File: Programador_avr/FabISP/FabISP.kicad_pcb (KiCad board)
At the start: 2 copper layers, 43.5 x 25 mm, 18 parts, among them IC1 ATTINY44-SSU, M1 20MHz, M2 PINHD-1x02-SMD-HEADER, M3 MICRO-USB_1_64

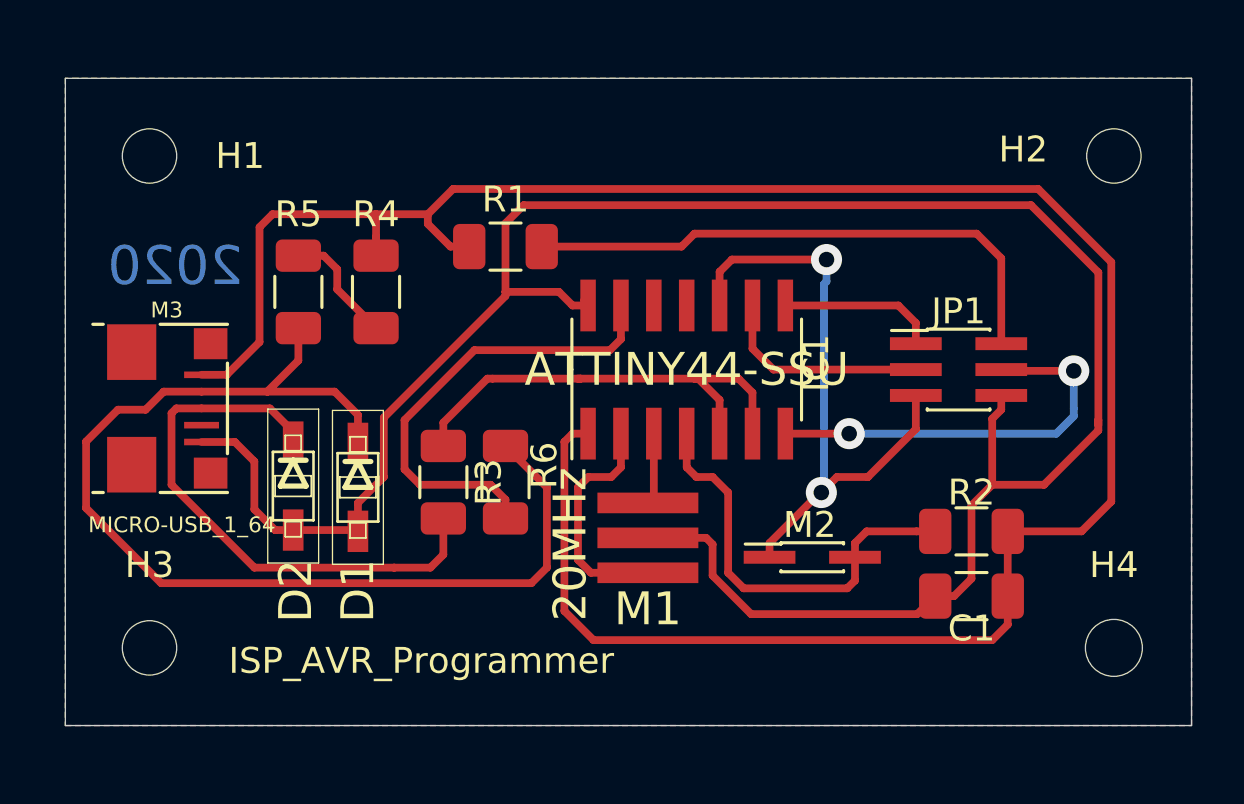
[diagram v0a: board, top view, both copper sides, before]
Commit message: comentatios DWgs, Corrección de margendes
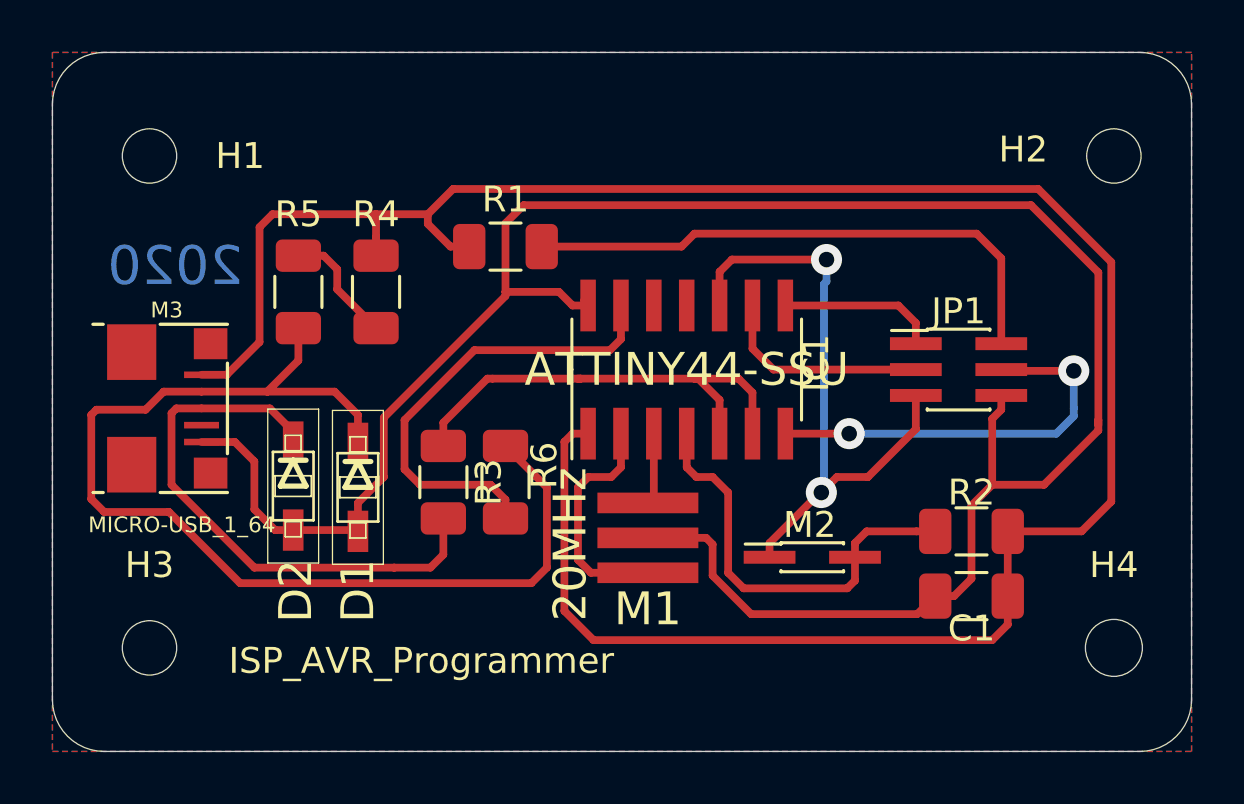
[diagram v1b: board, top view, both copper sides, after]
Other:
- board size 43.5 x 25 mm -> 44 x 27 mm
- rule trace_min: 0.2 -> 0.25
- board text added: "Vía 1.2mm/0.6mm"
- board text added: "grilla de borde : 1mm grilla de componentes: 0.25mm grilla pistas 0.25mm"
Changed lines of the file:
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@@
   (general
     (thickness 1.6)
-    (drawings 8)
-    (tracks 176)
+    (drawings 15)
+    (tracks 178)
     (zones 0)
     (modules 18)
@@
   )
   (setup
-    (last_trace_width 0.25)
+    (last_trace_width 0.3)
     (user_trace_width 0.3)
     (trace_clearance 0.2)
     (zone_clearance 0.508)
     (zone_45_only no)
-    (trace_min 0.2)
+    (trace_min 0.25)
     (via_size 0.8)
     (via_drill 0.4)
@@
     (pad "" np_thru_hole circle (at 0 0) (size 2.1 2.1) (drill 2.1) (layers *.Cu *.Mask))
   )
-  (gr_line (start 125.5 84) (end 126 84) (layer Edge.Cuts) (width 0.05))
-  (gr_line (start 125.5 109) (end 125.5 84) (layer Edge.Cuts) (width 0.05))
-  (gr_line (start 126 109) (end 125.5 109) (layer Edge.Cuts) (width 0.05))
-  (gr_line (start 126 109) (end 169 109) (layer Edge.Cuts) (width 0.05))
-  (gr_line (start 169 84) (end 126 84) (layer Edge.Cuts) (width 0.05))
-  (gr_line (start 169 84) (end 169 109) (layer Edge.Cuts) (width 0.05))
+  (dimension 2 (width 0.15) (layer Dwgs.User)
+    (gr_text "2,000 mm" (at 168 114.3) (layer Dwgs.User)
+      (effects (font (size 1 1) (thickness 0.15)))
+    )
+    (feature1 (pts (xy 169 108) (xy 169 113.586421)))
+    (feature2 (pts (xy 167 108) (xy 167 113.586421)))
+    (crossbar (pts (xy 167 113) (xy 169 113)))
+    (arrow1a (pts (xy 169 113) (xy 167.873496 113.586421)))
+    (arrow1b (pts (xy 169 113) (xy 167.873496 112.413579)))
+    (arrow2a (pts (xy 167 113) (xy 168.126504 113.586421)))
+    (arrow2b (pts (xy 167 113) (xy 168.126504 112.413579)))
+  )
+  (dimension 27 (width 0.15) (layer Dwgs.User)
+    (gr_text "27,000 mm" (at 120.7 96.5 270) (layer Dwgs.User)
+      (effects (font (size 1 1) (thickness 0.15)))
+    )
+    (feature1 (pts (xy 127 110) (xy 121.413579 110)))
+    (feature2 (pts (xy 127 83) (xy 121.413579 83)))
+    (crossbar (pts (xy 122 83) (xy 122 110)))
+    (arrow1a (pts (xy 122 110) (xy 121.413579 108.873496)))
+    (arrow1b (pts (xy 122 110) (xy 122.586421 108.873496)))
+    (arrow2a (pts (xy 122 83) (xy 121.413579 84.126504)))
+    (arrow2b (pts (xy 122 83) (xy 122.586421 84.126504)))
+  )
+  (dimension 44 (width 0.15) (layer Dwgs.User)
+    (gr_text "44,000 mm" (at 147 80.7) (layer Dwgs.User)
+      (effects (font (size 1 1) (thickness 0.15)))
+    )
+    (feature1 (pts (xy 169 85) (xy 169 81.413579)))
+    (feature2 (pts (xy 125 85) (xy 125 81.413579)))
+    (crossbar (pts (xy 125 82) (xy 169 82)))
+    (arrow1a (pts (xy 169 82) (xy 167.873496 82.586421)))
+    (arrow1b (pts (xy 169 82) (xy 167.873496 81.413579)))
+    (arrow2a (pts (xy 125 82) (xy 126.126504 82.586421)))
+    (arrow2b (pts (xy 125 82) (xy 126.126504 81.413579)))
+  )
+  (gr_text "Vía 1.2mm/0.6mm" (at 179 93) (layer Dwgs.User)
+    (effects (font (size 1 1) (thickness 0.15)))
+  )
+  (gr_line (start 125 108) (end 125 85) (layer Edge.Cuts) (width 0.05))
+  (gr_line (start 167 110) (end 127 110) (layer Edge.Cuts) (width 0.05))
+  (gr_line (start 169 85) (end 169 108) (layer Edge.Cuts) (width 0.05))
+  (gr_line (start 127 83) (end 167 83) (layer Edge.Cuts) (width 0.05))
+  (gr_arc (start 167 85) (end 169 85) (angle -90) (layer Edge.Cuts) (width 0.05))
+  (gr_arc (start 167 108) (end 167 110) (angle -90) (layer Edge.Cuts) (width 0.05))
+  (gr_arc (start 127 85) (end 127 83) (angle -90) (layer Edge.Cuts) (width 0.05))
+  (gr_arc (start 127 108) (end 125 108) (angle -90) (layer Edge.Cuts) (width 0.05))
+  (gr_text "grilla de borde : 1mm\ngrilla de componentes: 0.25mm\ngrilla pistas 0.25mm" (at 172 85) (layer Dwgs.User)
+    (effects (font (size 1 1) (thickness 0.15)) (justify left))
+  )
   (gr_text 2020 (at 129.75 91.25) (layer B.Cu)
     (effects (font (size 1.5 1.5) (thickness 0.3)) (justify mirror))
@@
   (segment (start 134.5 94.9) (end 134.5 93.65) (width 0.3) (layer F.Cu) (net 16) (status 20))
   (segment (start 133.2977 96.1023) (end 134.5 94.9) (width 0.3) (layer F.Cu) (net 16))
-  (segment (start 142.5 98.2) (end 144.1 99.8) (width 0.3) (layer F.Cu) (net 16) (status 10))
-  (segment (start 144.1 99.8) (end 144.1 102.9) (width 0.3) (layer F.Cu) (net 16))
-  (segment (start 144.1 102.9) (end 143.5 103.5) (width 0.3) (layer F.Cu) (net 16))
-  (segment (start 129.2 103.5) (end 126.3 100.6) (width 0.3) (layer F.Cu) (net 16))
-  (segment (start 143.5 103.5) (end 129.2 103.5) (width 0.3) (layer F.Cu) (net 16))
-  (segment (start 126.3 98.031959) (end 127.531959 96.8) (width 0.3) (layer F.Cu) (net 16))
-  (segment (start 126.3 100.6) (end 126.3 98.031959) (width 0.3) (layer F.Cu) (net 16))
-  (segment (start 127.531959 96.8) (end 128.6 96.8) (width 0.3) (layer F.Cu) (net 16))
-  (segment (start 129.2977 96.1023) (end 130.759581 96.1023) (width 0.3) (layer F.Cu) (net 16) (status 20))
-  (segment (start 128.6 96.8) (end 129.2977 96.1023) (width 0.3) (layer F.Cu) (net 16))
   (segment (start 135.90113 96.1023) (end 133.2977 96.1023) (width 0.3) (layer F.Cu) (net 16))
   (segment (start 136.8 97.00117) (end 135.90113 96.1023) (width 0.3) (layer F.Cu) (net 16))
   (segment (start 136.8 98.1) (end 136.8 97.00117) (width 0.3) (layer F.Cu) (net 16) (status 10))
+  (segment (start 129.2977 96.1023) (end 130.759581 96.1023) (width 0.3) (layer F.Cu) (net 16))
+  (segment (start 144.1 102.9) (end 143.5 103.5) (width 0.3) (layer F.Cu) (net 16))
+  (segment (start 132.25 103.5) (end 129.5 100.75) (width 0.3) (layer F.Cu) (net 16))
+  (segment (start 128.6 96.8) (end 129.2977 96.1023) (width 0.3) (layer F.Cu) (net 16))
+  (segment (start 126.5 100.25) (end 126.5 97) (width 0.3) (layer F.Cu) (net 16))
+  (segment (start 129.5 100.75) (end 127 100.75) (width 0.3) (layer F.Cu) (net 16))
+  (segment (start 142.5 98.2) (end 144.1 99.8) (width 0.3) (layer F.Cu) (net 16))
+  (segment (start 143.5 103.5) (end 132.25 103.5) (width 0.3) (layer F.Cu) (net 16))
+  (segment (start 126.7 96.8) (end 128.6 96.8) (width 0.3) (layer F.Cu) (net 16))
+  (segment (start 126.5 97) (end 126.7 96.8) (width 0.3) (layer F.Cu) (net 16))
+  (segment (start 127 100.75) (end 126.5 100.25) (width 0.3) (layer F.Cu) (net 16))
+  (segment (start 144.1 99.8) (end 144.1 102.9) (width 0.3) (layer F.Cu) (net 16))
   (segment (start 134.3 97.65069) (end 134.3 98.05074) (width 0.3) (layer F.Cu) (net 17) (status 30))
   (segment (start 133.39931 96.75) (end 134.3 97.65069) (width 0.3) (layer F.Cu) (net 17) (status 20))
@@
     (polygon
       (pts
-        (xy 125.5 84) (xy 125.5 109) (xy 169 109) (xy 169 84)
+        (xy 125 83) (xy 125 110) (xy 169 110) (xy 169 83)
       )
     )
@@
     (polygon
       (pts
-        (xy 125.5 84) (xy 125.5 109) (xy 169 109) (xy 169 84)
+        (xy 125 83) (xy 125 110) (xy 169 110) (xy 169 83)
       )
     )

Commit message: fiduciales y mejora de distribución
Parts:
- added FID2: Fiducial, Fiducial:Fiducial_1mm_Mask2mm, F.Cu at (160.0, 91.5)
- added FIDe: Fiducial, Fiducial:Fiducial_1mm_Mask2mm, B.Cu at (134.5, 86.8)
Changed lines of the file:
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@@
     (tracks 178)
     (zones 0)
-    (modules 18)
+    (modules 20)
     (nets 18)
   )
@@
     (mod_text_size 1 1)
     (mod_text_width 0.15)
-    (pad_size 2.1 2.1)
-    (pad_drill 2.1)
+    (pad_size 1 1)
+    (pad_drill 0)
     (pad_to_mask_clearance 0.051)
     (solder_mask_min_width 0.25)
@@
     (uvia_drill 0.1)
   )
+  (module Fiducial:Fiducial_1mm_Mask2mm (layer F.Cu)
+    (at 160 91.5)
+    (descr "Circular Fiducial, 1mm bare copper, 2mm soldermask opening (Level A)")
+    (tags fiducial)
+    (attr smd)
+    (fp_text reference FID2 (at 0 -2) (layer F.SilkS)
+      (effects (font (size 1 1) (thickness 0.15)))
+    )
+    (fp_text value Fiducial (at 0 2) (layer F.Fab)
+      (effects (font (size 1 1) (thickness 0.15)))
+    )
+    (fp_circle (center 0 0) (end 1.25 0) (layer F.CrtYd) (width 0.05))
+    (fp_text user %R (at 0 0) (layer F.Fab)
+      (effects (font (size 0.4 0.4) (thickness 0.06)))
+    )
+    (fp_circle (center 0 0) (end 1 0) (layer F.Fab) (width 0.1))
+    (pad "" smd circle (at 0 0) (size 1 1) (layers F.Cu F.Mask)
+      (solder_mask_margin 0.5) (clearance 0.5))
+  )
+  (module Fiducial:Fiducial_1mm_Mask2mm (layer B.Cu)
+    (at 134.5 86.75)
+    (descr "Circular Fiducial, 1mm bare copper, 2mm soldermask opening (Level A)")
+    (tags fiducial)
+    (attr smd)
+    (fp_text reference FIDe (at 0 2) (layer B.SilkS)
+      (effects (font (size 1 1) (thickness 0.15)) (justify mirror))
+    )
+    (fp_text value Fiducial (at 0 -2) (layer B.Fab)
+      (effects (font (size 1 1) (thickness 0.15)) (justify mirror))
+    )
+    (fp_circle (center 0 0) (end 1.25 0) (layer B.CrtYd) (width 0.05))
+    (fp_text user %R (at 0 0) (layer B.Fab)
+      (effects (font (size 0.4 0.4) (thickness 0.06)) (justify mirror))
+    )
+    (fp_circle (center 0 0) (end 1 0) (layer B.Fab) (width 0.1))
+    (pad "" smd circle (at 0 0) (size 1 1) (layers F.Cu B.Mask)
+      (solder_mask_margin 0.5) (clearance 0.5))
+  )
   (module MountingHole:MountingHole_2.1mm (layer F.Cu)
     (at 128.75 106)
@@
     (tags "SMALL OUTLINE DIODE")
     (attr smd)
-    (fp_text reference D2 (at 4.05 -0.1 90) (layer F.SilkS)
+    (fp_text reference D2 (at 4.05 -0.1 180) (layer F.SilkS)
       (effects (font (size 1.27 1.27) (thickness 0.1016)))
     )
@@
     (tags "SMALL OUTLINE DIODE")
     (attr smd)
-    (fp_text reference D1 (at 4.00074 0 90) (layer F.SilkS)
+    (fp_text reference D1 (at 4.00074 0 180) (layer F.SilkS)
       (effects (font (size 1.27 1.27) (thickness 0.1016)))
     )
@@
     (tags "Surface mounted pin header SMD 2x03 1.00mm double row")
     (attr smd)
-    (fp_text reference JP1 (at 0 -2.25) (layer F.SilkS)
+    (fp_text reference JP1 (at 0 2.75) (layer F.SilkS)
       (effects (font (size 1 1) (thickness 0.15)))
     )
@@
     (tags resistor)
     (attr smd)
-    (fp_text reference R3 (at 0 1.75 90) (layer F.SilkS)
+    (fp_text reference R3 (at -3.15 -0.1) (layer F.SilkS)
       (effects (font (size 1 1) (thickness 0.15)))
     )
@@
     (tags resistor)
     (attr smd)
-    (fp_text reference R6 (at -0.65 -1.5 90) (layer F.SilkS)
-      (effects (font (size 1 1) (thickness 0.15)))
-    )
+    (fp_text reference R6 (at 3.15 0) (layer F.SilkS)
+      (effects (font (size 1 1) (thickness 0.15)))
+    )

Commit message: Diseño para revisión
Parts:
- turned FIDe to 180 degrees
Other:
- board text added: "Mayer 10mls grilla de borde : 1mm grilla de componentes: 0.25mm grilla pistas 0.25mm margen: 0.25mm pista 0.3mm terminación: HASL"
- board text removed: "grilla de borde : 1mm grilla de componentes: 0.25mm grilla pistas 0.25mm"
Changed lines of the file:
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@@
   )
   (module Fiducial:Fiducial_1mm_Mask2mm (layer B.Cu)
-    (at 134.5 86.75)
+    (at 134.5 86.75 180)
     (descr "Circular Fiducial, 1mm bare copper, 2mm soldermask opening (Level A)")
     (tags fiducial)
@@
       (effects (font (size 1 1) (thickness 0.15)) (justify mirror))
     )
-    (fp_text value Fiducial (at 0 -2) (layer B.Fab)
+    (fp_text value Fiducial (at 0 -2) (layer B.Fab) hide
       (effects (font (size 1 1) (thickness 0.15)) (justify mirror))
     )
     (fp_circle (center 0 0) (end 1.25 0) (layer B.CrtYd) (width 0.05))
-    (fp_text user %R (at 0 0) (layer B.Fab)
+    (fp_text user %R (at 0 0) (layer B.Fab) hide
       (effects (font (size 0.4 0.4) (thickness 0.06)) (justify mirror))
     )
     (fp_circle (center 0 0) (end 1 0) (layer B.Fab) (width 0.1))
-    (pad "" smd circle (at 0 0) (size 1 1) (layers F.Cu B.Mask)
+    (pad "" smd circle (at 0 0 180) (size 1 1) (layers F.Cu B.Mask)
       (solder_mask_margin 0.5) (clearance 0.5))
   )
@@
       (effects (font (size 1 1) (thickness 0.15)))
     )
-    (fp_text value ATTINY44-SSU (at 0 0 180) (layer F.SilkS)
+    (fp_text value ATTINY44-SSU (at 0 0 180) (layer F.SilkS) hide
       (effects (font (size 1.27 1.27) (thickness 0.15)))
     )
@@
       (effects (font (size 1.27 1.27) (thickness 0.15)))
     )
-    (fp_text value 20MHz (at -0.25 -3 90) (layer F.SilkS)
+    (fp_text value 20MHz (at -0.25 -3 90) (layer F.SilkS) hide
       (effects (font (size 1.27 1.27) (thickness 0.15)))
     )
@@
       (effects (font (size 0.6096 0.6096) (thickness 0.0508)))
     )
-    (fp_text value MICRO-USB_1_64 (at 4.5 -0.838079) (layer F.SilkS)
+    (fp_text value MICRO-USB_1_64 (at 4.5 -0.838079) (layer F.SilkS) hide
       (effects (font (size 0.6096 0.6096) (thickness 0.0508)))
     )
@@
     (tags capacitor)
     (attr smd)
-    (fp_text reference C1 (at 0 -1.25) (layer F.SilkS)
+    (fp_text reference C1 (at 0 -2.25) (layer F.SilkS)
       (effects (font (size 1 1) (thickness 0.15)))
     )
@@
     (fp_line (start 3.65 2) (end 3.65 -2) (layer F.CrtYd) (width 0.05))
     (fp_line (start 3.65 -2) (end -3.65 -2) (layer F.CrtYd) (width 0.05))
-    (fp_text user %R (at 0 0 90) (layer F.Fab)
+    (fp_text user %R (at 0 0 90) (layer F.Fab) hide
       (effects (font (size 1 1) (thickness 0.15)))
     )
@@
     (tags resistor)
     (attr smd)
-    (fp_text reference R2 (at 0 1.5) (layer F.SilkS)
+    (fp_text reference R2 (at 0 2) (layer F.SilkS)
       (effects (font (size 1 1) (thickness 0.15)))
     )
@@
     (arrow2b (pts (xy 125 82) (xy 126.126504 81.413579)))
   )
-  (gr_text "Vía 1.2mm/0.6mm" (at 179 93) (layer Dwgs.User)
+  (gr_text "Vía 1.2mm/0.6mm" (at 179 99.5) (layer Dwgs.User)
     (effects (font (size 1 1) (thickness 0.15)))
   )
@@
   (gr_arc (start 127 85) (end 127 83) (angle -90) (layer Edge.Cuts) (width 0.05))
   (gr_arc (start 127 108) (end 125 108) (angle -90) (layer Edge.Cuts) (width 0.05))
-  (gr_text "grilla de borde : 1mm\ngrilla de componentes: 0.25mm\ngrilla pistas 0.25mm" (at 172 85) (layer Dwgs.User)
+  (gr_text "Mayer 10mls\ngrilla de borde : 1mm\ngrilla de componentes: 0.25mm\ngrilla pistas 0.25mm\nmargen: 0.25mm\npista 0.3mm\nterminación: HASL" (at 171.75 92.5) (layer Dwgs.User)
     (effects (font (size 1 1) (thickness 0.15)) (justify left))
   )
